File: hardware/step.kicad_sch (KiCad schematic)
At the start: 51 parts, among them J101 Cortex, J102 WAGO 2065-100, J103 WAGO 2065-100, SW101 SKSG, SW102 SKSG, U101 TPS78433QWDRBRQ1, U102 ATSAMD51J, Y101 32k768

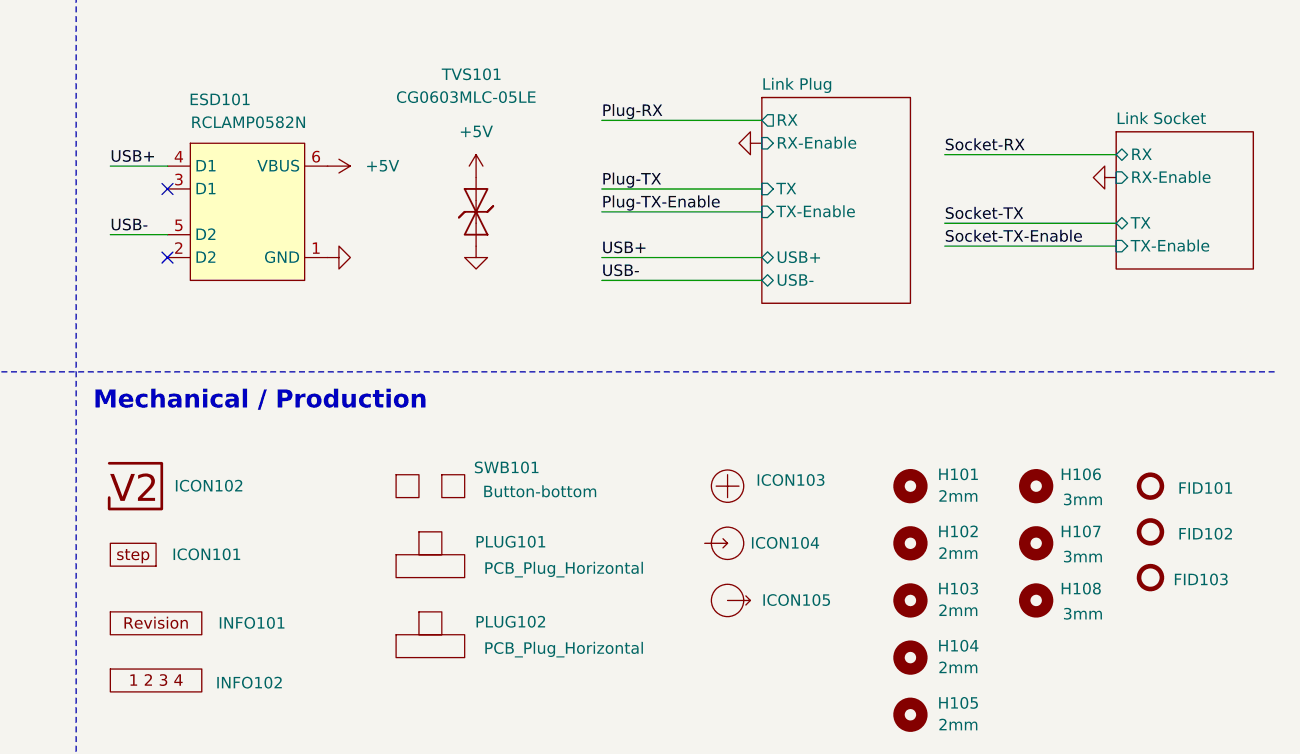
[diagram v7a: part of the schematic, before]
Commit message: Switch to 6 layer
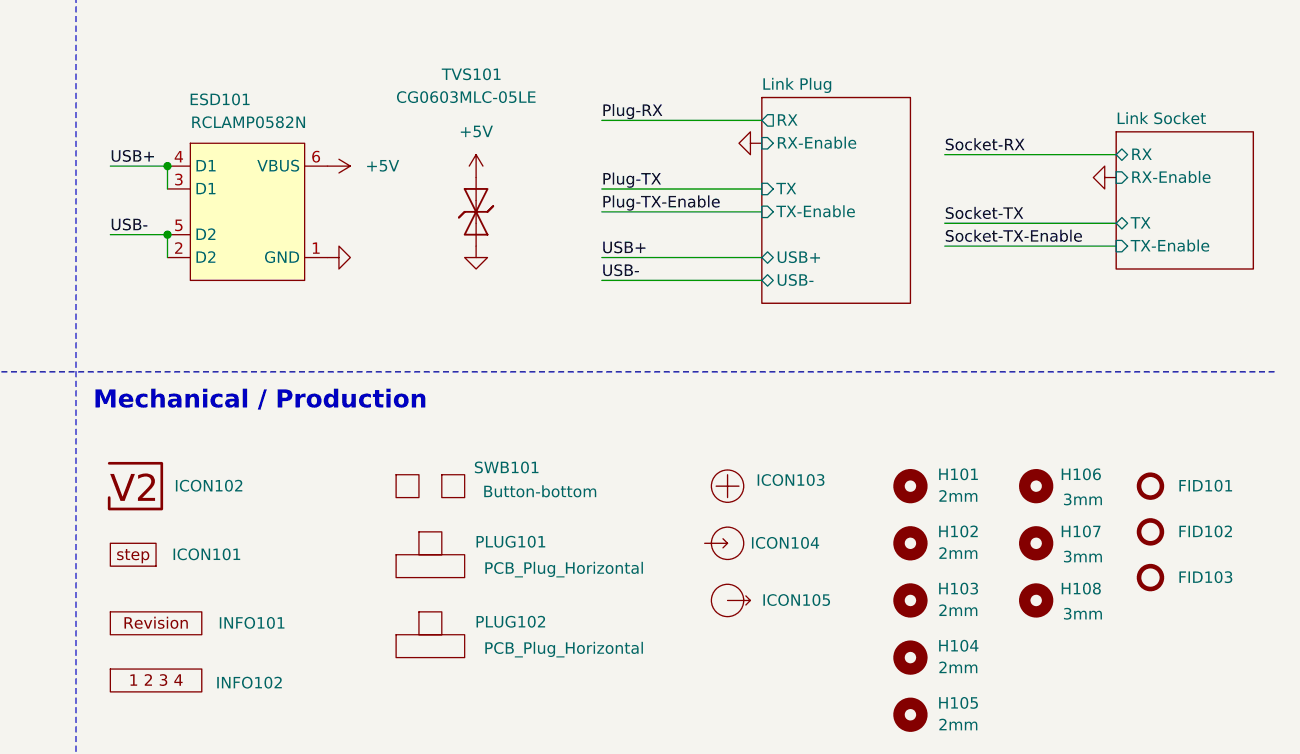
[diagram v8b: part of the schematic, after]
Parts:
- INFO102: value Layer_Numbers -> Layer_Numbers-6; footprint V2_Production:Layer_Numbers -> V2_Production:Layer_Numbers-6; symbol V2_Production:Layer_Numbers -> V2_Production:Layer_Numbers-6
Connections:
- net USB+: now also ESD101.3 (D1)
- net USB-: now also ESD101.2 (D2)
- no-connect marks 25 -> 23
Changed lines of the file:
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@@
 	(title_block
 		(title "V2 step")
-		(date "2026-05-08")
-		(rev "2026-02-10")
+		(date "2026-05-26")
+		(rev "2026-05-26")
 		(company "Versio Duo")
 		(comment 1 "Stepper Motor Controller")
@@
 	)
 	(junction
+		(at 161.29 116.84)
+		(diameter 0)
+		(color 0 0 0 0)
+	)
+	(junction
 		(at 88.9 21.59)
 		(diameter 0)
@@
 	)
 	(junction
+		(at 161.29 124.46)
+		(diameter 0)
+		(color 0 0 0 0)
+	)
+	(junction
 		(at 261.62 66.04)
 		(diameter 0)
@@
 	)
 	(no_connect
-		(at 161.29 127)
-	)
-	(no_connect
 		(at 133.35 180.34)
 	)
 	(no_connect
-		(at 161.29 119.38)
-	)
-	(no_connect
 		(at 53.34 55.88)
 	)
@@
 	(wire
 		(pts
+			(xy 161.29 116.84) (xy 161.29 119.38)
+		)
+		(stroke
+			(width 0)
+			(type default)
+		)
+	)
+	(wire
+		(pts
 			(xy 243.84 66.04) (xy 254 66.04)
 		)
@@
 	(wire
 		(pts
+			(xy 161.29 124.46) (xy 161.29 127)
+		)
+		(stroke
+			(width 0)
+			(type default)
+		)
+	)
+	(wire
+		(pts
 			(xy 110.49 86.36) (xy 125.73 86.36)
 		)
@@
 		(unit 1)
 		(body_style 1)
-		(exclude_from_sim no)
+		(exclude_from_sim yes)
 		(in_bom no)
 		(on_board yes)
@@
 			)
 		)
+		(property "Sim.Pins" "1=K 2=A"
+			(at 128.27 109.22 0)
+			(hide yes)
+			(show_name no)
+			(do_not_autoplace no)
+			(effects
+				(font
+					(size 1.27 1.27)
+				)
+			)
+		)
 		(pin "1"
 		)
@@
 		(unit 1)
 		(body_style 1)
-		(exclude_from_sim no)
+		(exclude_from_sim yes)
 		(in_bom no)
 		(on_board yes)
@@
 		(unit 1)
 		(body_style 1)
-		(exclude_from_sim no)
+		(exclude_from_sim yes)
 		(in_bom no)
 		(on_board yes)
@@
 		(unit 1)
 		(body_style 1)
-		(exclude_from_sim no)
+		(exclude_from_sim yes)
 		(in_bom no)
 		(on_board yes)
@@
 	)
 	(symbol
-		(lib_id "V2_Production:Layer_Numbers")
+		(lib_id "V2_Production:Layer_Numbers-6")
 		(at 160.02 173.99 0)
 		(unit 1)
@@
 			)
 		)
-		(property "Value" "Layer_Numbers"
+		(property "Value" "Layer_Numbers-6"
 			(at 159.4184 170.5185 0)
 			(hide yes)
@@
 			)
 		)
-		(property "Footprint" "V2_Production:Layer_Numbers"
+		(property "Footprint" "V2_Production:Layer_Numbers-6"
 			(at 160.02 180.34 0)
 			(hide yes)
@@
 		(dnp no)
 		(property "Reference" "FID101"
-			(at 273.558 152.654 0)
+			(at 273.558 152.4 0)
 			(show_name no)
 			(do_not_autoplace no)
@@
 		(unit 1)
 		(body_style 1)
-		(exclude_from_sim no)
+		(exclude_from_sim yes)
 		(in_bom no)
 		(on_board yes)
@@
 		(dnp no)
 		(property "Reference" "FID102"
-			(at 273.558 157.734 0)
+			(at 273.558 157.48 0)
 			(show_name no)
 			(do_not_autoplace no)
@@
 		(unit 1)
 		(body_style 1)
-		(exclude_from_sim no)
+		(exclude_from_sim yes)
 		(in_bom no)
 		(on_board yes)
@@
 		(dnp no)
 		(property "Reference" "FID103"
-			(at 273.05 162.814 0)
+			(at 273.558 162.56 0)
 			(show_name no)
 			(do_not_autoplace no)
@@
 		(unit 1)
 		(body_style 1)
-		(exclude_from_sim no)
+		(exclude_from_sim yes)
 		(in_bom no)
 		(on_board yes)
